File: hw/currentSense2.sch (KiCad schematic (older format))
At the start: 2 parts, among them U1301 ZXCT1086

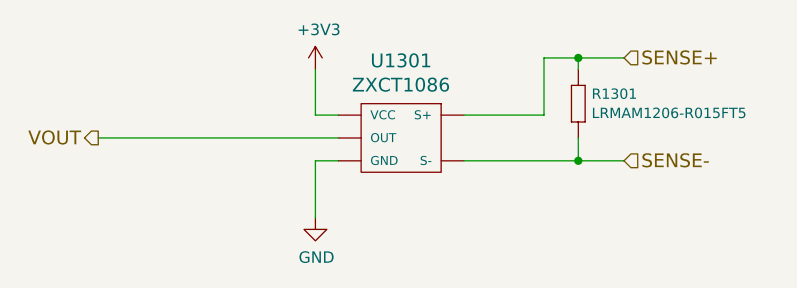
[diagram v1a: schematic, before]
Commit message: added binary and build files to gitignore
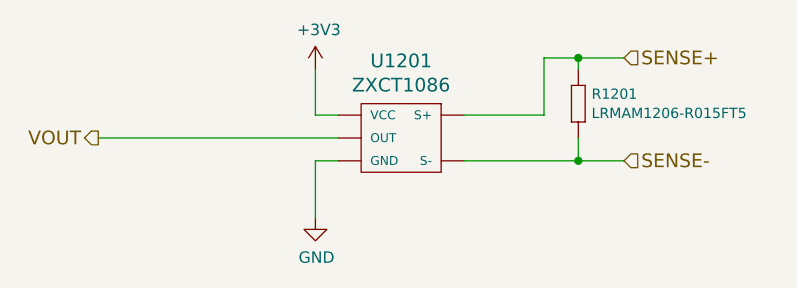
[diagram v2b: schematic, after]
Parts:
- renumbered U1301 to U701
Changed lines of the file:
@@
 $EndDescr
 $Comp
-L ZXCT1086 U1301
+L ZXCT1086 U701
 U 1 1 589841A1
 P 5450 3600
-F 0 "U1301" H 5425 3887 60  0000 C CNN
+AR Path="/58BE52C9/5955DE03/589841A1" Ref="U701"  Part="1"
+AR Path="/58BE52C9/59B27EDC/589841A1" Ref="U801"  Part="1"
+AR Path="/58C7B0A8/58BE8E88/589841A1" Ref="U1201"  Part="1"
+AR Path="/58C7B0A8/58BE8E96/589841A1" Ref="U1301"  Part="1"
+F 0 "U1201" H 5425 3887 60  0000 C CNN
 F 1 "ZXCT1086" H 5425 3781 60  0000 C CNN
 F 2 "usevolt:SOT-25" H 5100 4050 60  0001 C CNN
@@
 $EndComp
 $Comp
-L GND #PWR044
+L GND #PWR030
 U 1 1 589841A8
 P 5050 4000
-F 0 "#PWR044" H 5050 3750 50  0001 C CNN
+AR Path="/58BE52C9/5955DE03/589841A8" Ref="#PWR030"  Part="1"
+AR Path="/58BE52C9/59B27EDC/589841A8" Ref="#PWR032"  Part="1"
+AR Path="/58C7B0A8/58BE8E88/589841A8" Ref="#PWR041"  Part="1"
+AR Path="/58C7B0A8/58BE8E96/589841A8" Ref="#PWR043"  Part="1"
+F 0 "#PWR041" H 5050 3750 50  0001 C CNN
 F 1 "GND" H 5055 3827 50  0000 C CNN
 F 2 "" H 5050 4000 50  0000 C CNN
@@
 $EndComp
 $Comp
-L +3V3 #PWR045
+L +3V3 #PWR031
 U 1 1 594D8B7F
 P 5050 3350
-F 0 "#PWR045" H 5050 3200 50  0001 C CNN
+AR Path="/58BE52C9/5955DE03/594D8B7F" Ref="#PWR031"  Part="1"
+AR Path="/58BE52C9/59B27EDC/594D8B7F" Ref="#PWR033"  Part="1"
+AR Path="/58C7B0A8/58BE8E88/594D8B7F" Ref="#PWR042"  Part="1"
+AR Path="/58C7B0A8/58BE8E96/594D8B7F" Ref="#PWR044"  Part="1"
+F 0 "#PWR042" H 5050 3200 50  0001 C CNN
 F 1 "+3V3" H 5065 3523 50  0000 C CNN
 F 2 "" H 5050 3350 50  0000 C CNN
@@
 U 1 1 59550A4F
 P 6200 3450
-F 0 "R1301" V 6208 3508 45  0000 L CNN
+AR Path="/58C7B0A8/58BE8E96/59550A4F" Ref="R1301"  Part="1"
+AR Path="/58BE52C9/5955DE03/59550A4F" Ref="R701"  Part="1"
+AR Path="/58BE52C9/59B27EDC/59550A4F" Ref="R801"  Part="1"
+AR Path="/58C7B0A8/58BE8E88/59550A4F" Ref="R1201"  Part="1"
+F 0 "R1201" V 6208 3508 45  0000 L CNN
 F 1 "LRMAM1206-R015FT5" V 6292 3508 45  0000 L CNN
 F 2 "usevolt:1206" H 6230 3600 20  0001 C CNN

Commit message: 3.0.0 ready to order
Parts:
- removed U701: ZXCT1086, usevolt:SOT-25, symbol ZXCT1086
- added U1201: ZXCT1086, usevolt:SOT-25, symbol ZXCT1086
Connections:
- net +3V3: now also U1201.5 (VCC)
- net GND: now also U1201.2 (GND)
- net SENSE+: now also U1201.3 (S+)
- net SENSE-: now also U1201.4 (S-)
- net VOUT: now also U1201.1 (OUT)
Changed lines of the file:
@@
 EESchema Schematic File Version 2
+LIBS:esb-rescue
 LIBS:kemet
-LIBS:multicomp
 LIBS:usevolt
 LIBS:wurth_elektronik_LED
 LIBS:power
 LIBS:elt21300_kicad
+LIBS:yageo
 LIBS:esb-cache
 EELAYER 26 0
@@
 $EndDescr
 $Comp
-L ZXCT1086 U701
-U 1 1 589841A1
+L ZXCT1086 U1201
+U 1 1 59B98AFC
 P 5450 3600
-AR Path="/58BE52C9/5955DE03/589841A1" Ref="U701"  Part="1"
-AR Path="/58BE52C9/59B27EDC/589841A1" Ref="U801"  Part="1"
-AR Path="/58C7B0A8/58BE8E88/589841A1" Ref="U1201"  Part="1"
-AR Path="/58C7B0A8/58BE8E96/589841A1" Ref="U1301"  Part="1"
-F 0 "U1201" H 5425 3887 60  0000 C CNN
+AR Path="/58C7B0A8/58BE8E88/59B98AFC" Ref="U1201"  Part="1"
+AR Path="/58C7B0A8/58BE8E96/59B98AFC" Ref="U1301"  Part="1"
+F 0 "U1301" H 5425 3887 60  0000 C CNN
 F 1 "ZXCT1086" H 5425 3781 60  0000 C CNN
 F 2 "usevolt:SOT-25" H 5100 4050 60  0001 C CNN
@@
 $EndComp
 $Comp
-L GND #PWR030
+L GND #PWR1202
 U 1 1 589841A8
 P 5050 4000
-AR Path="/58BE52C9/5955DE03/589841A8" Ref="#PWR030"  Part="1"
-AR Path="/58BE52C9/59B27EDC/589841A8" Ref="#PWR032"  Part="1"
-AR Path="/58C7B0A8/58BE8E88/589841A8" Ref="#PWR041"  Part="1"
-AR Path="/58C7B0A8/58BE8E96/589841A8" Ref="#PWR043"  Part="1"
-F 0 "#PWR041" H 5050 3750 50  0001 C CNN
+AR Path="/58C7B0A8/58BE8E88/589841A8" Ref="#PWR1202"  Part="1"
+AR Path="/58C7B0A8/58BE8E96/589841A8" Ref="#PWR1302"  Part="1"
+F 0 "#PWR1302" H 5050 3750 50  0001 C CNN
 F 1 "GND" H 5055 3827 50  0000 C CNN
 F 2 "" H 5050 4000 50  0000 C CNN
@@
 $EndComp
 $Comp
-L +3V3 #PWR031
+L +3V3 #PWR1201
 U 1 1 594D8B7F
 P 5050 3350
-AR Path="/58BE52C9/5955DE03/594D8B7F" Ref="#PWR031"  Part="1"
-AR Path="/58BE52C9/59B27EDC/594D8B7F" Ref="#PWR033"  Part="1"
-AR Path="/58C7B0A8/58BE8E88/594D8B7F" Ref="#PWR042"  Part="1"
-AR Path="/58C7B0A8/58BE8E96/594D8B7F" Ref="#PWR044"  Part="1"
-F 0 "#PWR042" H 5050 3200 50  0001 C CNN
+AR Path="/58C7B0A8/58BE8E88/594D8B7F" Ref="#PWR1201"  Part="1"
+AR Path="/58C7B0A8/58BE8E96/594D8B7F" Ref="#PWR1301"  Part="1"
+F 0 "#PWR1301" H 5050 3200 50  0001 C CNN
 F 1 "+3V3" H 5065 3523 50  0000 C CNN
 F 2 "" H 5050 3350 50  0000 C CNN
@@
 $Comp
 L LRMAM1206-R015FT5 R1301
-U 1 1 59550A4F
+U 1 1 59B972DD
 P 6200 3450
-AR Path="/58C7B0A8/58BE8E96/59550A4F" Ref="R1301"  Part="1"
-AR Path="/58BE52C9/5955DE03/59550A4F" Ref="R701"  Part="1"
-AR Path="/58BE52C9/59B27EDC/59550A4F" Ref="R801"  Part="1"
-AR Path="/58C7B0A8/58BE8E88/59550A4F" Ref="R1201"  Part="1"
-F 0 "R1201" V 6208 3508 45  0000 L CNN
+AR Path="/58C7B0A8/58BE8E96/59B972DD" Ref="R1301"  Part="1"
+AR Path="/58BE52C9/59B27EDC/59B972DD" Ref="R?"  Part="1"
+AR Path="/58C7B0A8/58BE8E88/59B972DD" Ref="R1201"  Part="1"
+F 0 "R1301" V 6208 3508 45  0000 L CNN
 F 1 "LRMAM1206-R015FT5" V 6292 3508 45  0000 L CNN
 F 2 "usevolt:1206" H 6230 3600 20  0001 C CNN
